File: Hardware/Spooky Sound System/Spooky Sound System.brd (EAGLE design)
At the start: 101.6 x 36.5 mm, 18 parts, among them U1 LM3886TF/NOPB, U2 LM3886TF/NOPB, U3 LM3886TF/NOPB

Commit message: tone control done.
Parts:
- added C10, C17: 220nF, MF_Passives:C0805
- added C11, C18: 47uF, MF_Passives:CP6.3MM
- added C12, C13, C19: 10uF, MF_Passives:CP4MM
- added C14, C7: 2.2nF, MF_Passives:C0805
- added C15, C16, C8, C9: 22nF, MF_Passives:C0805
- added P1, P2, P3: 100K, PP_Passives:DUAL_TAPER_POTENTIOMETER
- added R10: 12K, MF_Passives:R0805
- added R11, R12: 100K, MF_Passives:R0805
- C1, C3, C5: value 47uF -> 0.1uF; device MF_Passives:C0805 -> MF_Passives:C1206
- C2, C4: value 100uF -> 0.1uF; device MF_Passives:CP6.3MM -> MF_Passives:C1206
- C6: value 100uF -> 10uF; device MF_Passives:CP6.3MM -> MF_Passives:CP4MM
- R1, R7: value 1K -> 10K
- R2, R8: value 22K -> 10K
- R3, R9: value 22K -> 4.7K
- R4: value 1K -> 12K
- R5, R6: value 22K -> 100K
- U1: value LM3886TF/NOPB -> TDA7387; device PP_AnalogIC:LM388TF-TO-220-11 -> PP_AnalogIC:TDA7387-FLEXIWATT-25
- U2, U3: value LM3886TF/NOPB -> AZ4558C; device PP_AnalogIC:LM388TF-TO-220-11 -> PP_AnalogIC:AZ4558C_SOIC-8
- moved R7 189.5 mm to (-38.1, -118.1)
- moved U3 180.0 mm to (-31.8, -109.2)
- moved R8 168.1 mm to (-33.0, -118.1)
- moved R9 168.1 mm to (-27.9, -118.1)
- moved C6 100.2 mm to (-3.81, -36.8)
- moved C5 99.6 mm to (2.54, -31.8)
- moved R4 95.6 mm to (-3.81, -54.6)
- moved R6 87.1 mm to (-3.81, -62.2)
- moved R5 81.1 mm to (-3.81, -58.4)
- moved U2 77.8 mm to (6.35, -38.1)
- moved R3 72.4 mm to (-3.81, -50.8)
- moved R2 70.3 mm to (-3.81, -47.0)
- moved C3 64.9 mm to (2.54, -22.9)
- moved C4 60.2 mm to (2.54, -26.7)
- moved R1 53.3 mm to (-3.81, -43.2)
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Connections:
- removed net V+: C2.P$1, C4.P$1, C6.P$1, U1.P$1, U1.P$5, U2.P$1, U2.P$5, U3.P$1, U3.P$5
- new net AC-GND: C5.P$2, U1.P$16
- new net IN_L: U2.3
- new net IN_R: U3.3
- new net N$11: C11.P$1, R5.P$2, R6.P$1, U2.5
- new net N$12: C13.P$2, U3.1, U3.2
- new net N$13: C13.P$1, C14.P$1, R7.P$1
- new net N$14: C16.P$1, P1.1B, R7.P$2
- new net N$15: C16.P$2, C17.P$1, P1.2B, R8.P$2
- new net N$16: C17.P$2, P1.3B, R10.P$2
- new net N$17: R8.P$1, R9.P$2, U3.6
- new net N$18: P2.2B, R9.P$1
- new net N$19: C14.P$2, P2.1B
- new net N$20: C15.P$1, P2.3B
- new net N$21: C15.P$2, C19.P$1, R10.P$1, U3.7
- new net N$22: C18.P$1, R11.P$2, R12.P$1, U3.5
- new net OUT_L: C12.P$2, P3.3A
- new net OUT_R: C19.P$2, P3.1B
- new net TDA7387_IN1: C1.P$2, U1.P$11
- new net TDA7387_IN2: C2.P$2, U1.P$12
- new net TDA7387_IN3: C3.P$2, U1.P$15
- new net TDA7387_IN4: C4.P$2, U1.P$14
- new net VIN: R11.P$1, R5.P$1, U2.8, U3.8
- net GND: now also C11.P$2, C18.P$2, P3.1A, P3.3B, R12.P$2, R6.P$2, U2.4, U3.4; no longer C1.P$2, C2.P$2, C3.P$2, C4.P$2, C5.P$2, C6.P$2, R2.P$2, R5.P$2, R8.P$2, U1.P$7, U1.P$8, U2.P$7, U2.P$8, U3.P$7, U3.P$8
- net N$1: now also C6.P$2, U2.1, U2.2; no longer R1.P$2, R2.P$1, U1.P$10
- net N$10: now also C12.P$1, C8.P$2, R4.P$1, U2.7; no longer C5.P$1, R9.P$2
- net N$2: now also C6.P$1, C7.P$1; no longer R4.P$1, R7.P$1
- net N$3: now also C9.P$1, P1.1A, R1.P$2; no longer R3.P$1, U1.P$9
- net N$4: now also C10.P$1, C9.P$2, P1.2A, R2.P$2; no longer C1.P$1, R3.P$2
- net N$5: now also C10.P$2, P1.3A; no longer R5.P$1, U2.P$10
- net N$6: now also R2.P$1, R3.P$2, U2.6; no longer R6.P$1, U2.P$9
- net N$7: now also P2.2A, R3.P$1; no longer C3.P$1, R6.P$2
- net N$8: now also C7.P$2, P2.1A; no longer R7.P$2, R8.P$1, U3.P$10
- net N$9: now also C8.P$1, P2.3A; no longer R9.P$1, U3.P$9

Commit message: Schematic done. Start Routing.
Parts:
- added C20, C21, C22, C23: 0.01uF, MF_Passives:C1210
- added C24: 22nF, MF_Passives:C0805
- added C25, C27, C28, C31: 10uF, MF_Passives:CP4MM
- added C26: 0.1uF, MF_Passives:C0805
- added C29, C30: 1000uF, MF_Passives:CP12.5MM
- added C32: 47uF, MF_Passives:CP6.3MM
- added C33, C34, C35: 100uF, MF_Passives:CP6.3MM
- added J1: SJ1-3533NS, PP_Connectors:SJ1-3533NS
- added J2, J3, J4: 1546215-2, PP_Connectors:1546215-2
- added P4, P5: 100K, PP_Passives:DUAL_TAPER_POTENTIOMETER
- added R13, R14, R19, R20: 1M, MF_Passives:R0805
- added R15, R16, R17, R18, R21, R22, R23, R24, R27, R30, R31, R32: 0, MF_Passives:R0805
- added R25, R26, R28, R29: 10K, MF_Passives:R0805
- added R33, R34: 220K, MF_Passives:R0805
- added R35: 1K, MF_Passives:R0805
- added U4, U5, U6: AZ4558C, PP_AnalogIC:AZ4558C_SOIC-8
- moved R11 215.6 mm to (96.5, 33.0), turned to 180 degrees
- moved C15 210.1 mm to (96.5, 29.2), turned to 180 degrees
- moved R12 208.6 mm to (91.4, 33.0), turned to 180 degrees
- moved C16 203.0 mm to (91.4, 29.2), turned to 180 degrees
- moved C18 197.9 mm to (95.2, 21.6), turned to 180 degrees
- moved C17 196.2 mm to (86.4, 29.2), turned to 180 degrees
- moved R7 189.6 mm to (81.3, 29.2), turned to 180 degrees
- moved C13 186.8 mm to (88.9, 20.3), turned to 180 degrees
- moved P3 183.7 mm to (83.8, 0.00), turned to 180 degrees
- moved R8 183.4 mm to (76.2, 29.2), turned to 180 degrees
- moved C19 179.6 mm to (83.8, 20.3), turned to 180 degrees
- moved R9 177.5 mm to (71.1, 29.2), turned to 180 degrees
- moved R10 172.1 mm to (66.0, 29.2), turned to 180 degrees
- moved U3 167.8 mm to (74.9, 20.3), turned to 180 degrees
- moved C11 164.0 mm to (95.2, 10.2), turned to 180 degrees
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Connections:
- new net AUD_IN_L: C20.P$1, C22.P$1, J1.2_A, J1.2_B
- new net AUD_IN_R: C21.P$1, C23.P$1, J1.3_A, J1.3_B
- new net L+: J2.P$1, U1.P$9
- new net L-: J2.P$2, U1.P$7
- new net N$23: C27.P$2, R21.P$2, U4.1
- new net N$24: P5.3A, R21.P$1
- new net N$25: P3.3B, R16.P$1
- new net N$26: P3.1B, R17.P$2
- new net N$27: C28.P$2, R23.P$2, U4.7
- new net N$28: P5.3B, R23.P$1
- new net N$29: C26.P$1, R25.P$2, R26.P$2, R28.P$1, U5.2
- new net N$30: C26.P$2, P4.3A, R28.P$2, U5.1
- new net N$31: R29.P$1, U5.3
- new net N$32: P4.2A, R31.P$2
- new net N$33: R30.P$2, R32.P$1, U5.6
- new net N$34: C25.P$1, R30.P$1, U5.7
- new net N$35: P5.2A, U4.2
- new net N$36: P5.1A, R22.P$2
- new net N$37: P5.1B, R24.P$2
- new net N$38: P5.2B, U4.6
- new net N$39: P3.2B, U3.2
- new net N$40: P3.3A, R18.P$2
- new net N$41: P3.2A, U2.2
- new net N$42: P3.1A, R15.P$1
- new net N$43: C24.P$1, R31.P$1, U5.5
- new net N$44: C25.P$2, R27.P$1
- new net N$45: C27.P$1, R26.P$1
- new net N$46: C28.P$1, R25.P$1
- new net N$47: C33.P$2, C34.P$1, R33.P$2, R34.P$1, U6.3
- new net N$48: R35.P$1, U6.1
- new net N$49: C32.P$1, U1.P$10
- new net OUT_SUB: C3.P$1, R27.P$2
- new net R+: J3.P$1, U1.P$5
- new net R-: J3.P$2, U1.P$3
- new net SUB+: J4.P$1, U1.P$17
- new net SUB-: J4.P$2, U1.P$19
- new net SUB_L: C22.P$2, R19.P$1
- new net SUB_R: C23.P$2, R20.P$1, U4.5
- new net VGND: C11.P$2, C18.P$2, C24.P$2, R12.P$2, R13.P$2, R14.P$2, R17.P$1, R18.P$1, R19.P$2, R20.P$2, R22.P$1, R24.P$1, R29.P$2, R32.P$2, R35.P$2, R6.P$2, U6.2
- net GND: now also C29.P$2, C30.P$2, C31.P$2, C32.P$2, C34.P$2, C35.P$2, C4.P$1, C5.P$1, J1.1_A, J1.1_B, J1.S1, J1.S2, J1.S3, J1.S4, J1.S5, J1.S6, R34.P$2, U1.P$1, U1.P$13, U1.P$18, U1.P$2, U1.P$24, U1.P$8, U4.4, U5.4, U6.4; no longer C11.P$2, C18.P$2, P3.1A, P3.3B, R12.P$2, R6.P$2
- net IN_L: now also C20.P$2, R14.P$1
- net IN_R: now also C21.P$2, R13.P$1
- net N$1: now also R15.P$2; no longer U2.2
- net N$12: now also R16.P$2; no longer U3.2
- net OUT_L: now also C1.P$1; no longer P3.3A
- net OUT_R: now also C2.P$1; no longer P3.1B
- net VIN: now also C29.P$1, C30.P$1, C31.P$1, C33.P$1, C35.P$1, R33.P$1, U1.P$20, U1.P$22, U1.P$4, U1.P$6, U4.8, U5.8, U6.8
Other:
- board size 101.6 x 36.5 mm -> 101.6 x 54.3 mm

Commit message: Starting layout...
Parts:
- added J5: 1546215-2, PP_Connectors:1546215-2
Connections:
- net GND: now also J5.P$2
- net VIN: now also J5.P$1
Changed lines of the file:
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@@
 <attribute name="MPN" value="" x="97.79" y="48.26" size="1.778" layer="27" rot="R180" display="off"/>
+</element>
+<element name="J5" library="PP_Connectors" package="1546215-2" value="1546215-2" x="3.81" y="50.8" rot="R180">
+<attribute name="URL" value="" x="3.81" y="50.8" size="1.778" layer="27" rot="R180" display="off"/>
+<attribute name="POPULATE" value="1" x="3.81" y="50.8" size="1.778" layer="27" rot="R180" display="off"/>
+<attribute name="LABEL02" value="GND" x="3.81" y="50.8" size="1.778" layer="27" rot="R180" display="off"/>
+<attribute name="HOUSEPART" value="" x="3.81" y="50.8" size="1.778" layer="27" rot="R180" display="off"/>
+<attribute name="LABEL01" value="VIN" x="3.81" y="50.8" size="1.778" layer="27" rot="R180" display="off"/>
+<attribute name="MPN" value="" x="3.81" y="50.8" size="1.778" layer="27" rot="R180" display="off"/>
 </element>
 </elements>
@@
 <contactref element="C30" pad="P$1"/>
 <contactref element="U1" pad="P$20"/>
-<wire x1="58.42" y1="36.99" x2="73.66" y2="36.99" width="0" layer="19" extent="1-1"/>
+<contactref element="J5" pad="P$1"/>
+<wire x1="90.805" y1="23.02" x2="97.47" y2="33.02" width="0" layer="19" extent="1-1"/>
+<wire x1="72.23" y1="18.415" x2="90.805" y2="23.02" width="0" layer="19" extent="1-1"/>
+<wire x1="61.214" y1="31.9278" x2="72.23" y2="18.415" width="0" layer="19" extent="1-1"/>
+<wire x1="59.182" y1="31.9278" x2="61.214" y2="31.9278" width="0" layer="19" extent="1-1"/>
+<wire x1="58.42" y1="36.99" x2="59.182" y2="31.9278" width="0" layer="19" extent="1-1"/>
+<wire x1="73.66" y1="36.99" x2="61.214" y2="31.9278" width="0" layer="19" extent="1-1"/>
 <wire x1="44.45" y1="37.31" x2="58.42" y2="36.99" width="0" layer="19" extent="1-1"/>
-<wire x1="34.29" y1="35.33" x2="44.45" y2="37.31" width="0" layer="19" extent="1-1"/>
-<wire x1="19.05" y1="31.52" x2="34.29" y2="35.33" width="0" layer="19" extent="1-1"/>
+<wire x1="44.958" y1="31.9278" x2="44.45" y2="37.31" width="0" layer="19" extent="1-1"/>
+<wire x1="42.926" y1="31.9278" x2="44.958" y2="31.9278" width="0" layer="19" extent="1-1"/>
+<wire x1="34.29" y1="35.33" x2="42.926" y2="31.9278" width="0" layer="19" extent="1-1"/>
+<wire x1="40.005" y1="23.02" x2="42.926" y2="31.9278" width="0" layer="19" extent="1-1"/>
+<wire x1="29.21" y1="20.64" x2="40.005" y2="23.02" width="0" layer="19" extent="1-1"/>
+<wire x1="19.05" y1="31.52" x2="29.21" y2="20.64" width="0" layer="19" extent="1-1"/>
 <wire x1="9.84" y1="30.48" x2="19.05" y2="31.52" width="0" layer="19" extent="1-1"/>
+<wire x1="6.985" y1="34.45" x2="9.84" y2="30.48" width="0" layer="19" extent="1-1"/>
 <wire x1="2.38" y1="23.495" x2="9.84" y2="30.48" width="0" layer="19" extent="1-1"/>
-<wire x1="90.805" y1="23.02" x2="2.38" y2="23.495" width="0" layer="19" extent="1-1"/>
-<wire x1="40.005" y1="23.02" x2="90.805" y2="23.02" width="0" layer="19" extent="1-1"/>
-<wire x1="97.47" y1="33.02" x2="40.005" y2="23.02" width="0" layer="19" extent="1-1"/>
-<wire x1="72.23" y1="18.415" x2="97.47" y2="33.02" width="0" layer="19" extent="1-1"/>
-<wire x1="29.21" y1="20.64" x2="72.23" y2="18.415" width="0" layer="19" extent="1-1"/>
-<wire x1="6.985" y1="34.45" x2="29.21" y2="20.64" width="0" layer="19" extent="1-1"/>
-<wire x1="44.958" y1="31.9278" x2="6.985" y2="34.45" width="0" layer="19" extent="1-1"/>
-<wire x1="42.926" y1="31.9278" x2="44.958" y2="31.9278" width="0" layer="19" extent="1-1"/>
-<wire x1="59.182" y1="31.9278" x2="44.958" y2="31.9278" width="0" layer="19" extent="1-1"/>
-<wire x1="61.214" y1="31.9278" x2="59.182" y2="31.9278" width="0" layer="19" extent="1-1"/>
+<wire x1="5.08" y1="50.8" x2="2.38" y2="23.495" width="0" layer="19" extent="1-1"/>
 </signal>
 <signal name="N$1">
@@
 <contactref element="J1" pad="1_A"/>
 <contactref element="J1" pad="1_B"/>
+<contactref element="J5" pad="P$2"/>
 <wire x1="71.04" y1="51.54" x2="71.04" y2="51.54" width="0" layer="19" extent="1-16"/>
 <wire x1="72.04" y1="47.39" x2="71.04" y2="51.54" width="0" layer="19" extent="1-16"/>
@@
 <wire x1="62.14" y1="42.94" x2="62.14" y2="51.54" width="0" layer="19" extent="1-16"/>
 <wire x1="62.14" y1="42.94" x2="62.14" y2="42.94" width="0" layer="19" extent="1-16"/>
-<wire x1="66.04" y1="31.59" x2="62.14" y2="42.94" width="0" layer="19" extent="1-16"/>
+<wire x1="63.246" y1="31.9278" x2="62.14" y2="42.94" width="0" layer="19" extent="16-16"/>
+<wire x1="66.04" y1="31.59" x2="63.246" y2="31.9278" width="0" layer="19" extent="1-1"/>
+<wire x1="57.15" y1="31.9278" x2="63.246" y2="31.9278" width="0" layer="19" extent="1-1"/>
+<wire x1="50.8" y1="31.59" x2="57.15" y2="31.9278" width="0" layer="19" extent="1-1"/>
+<wire x1="46.99" y1="31.9278" x2="50.8" y2="31.59" width="0" layer="19" extent="1-1"/>
+<wire x1="44.45" y1="33.81" x2="46.99" y2="31.9278" width="0" layer="19" extent="1-1"/>
+<wire x1="52.07" y1="27.94" x2="50.8" y2="31.59" width="0" layer="19" extent="1-1"/>
+<wire x1="40.894" y1="31.9278" x2="44.45" y2="33.81" width="0" layer="19" extent="1-1"/>
+<wire x1="39.878" y1="27.94" x2="40.894" y2="31.9278" width="0" layer="19" extent="1-1"/>
+<wire x1="34.29" y1="25.63" x2="39.878" y2="27.94" width="0" layer="19" extent="1-1"/>
 <wire x1="73.66" y1="31.59" x2="66.04" y2="31.59" width="0" layer="19" extent="1-1"/>
-<wire x1="50.8" y1="31.59" x2="66.04" y2="31.59" width="0" layer="19" extent="1-1"/>
-<wire x1="44.45" y1="33.81" x2="50.8" y2="31.59" width="0" layer="19" extent="1-1"/>
-<wire x1="34.29" y1="25.63" x2="44.45" y2="33.81" width="0" layer="19" extent="1-1"/>
+<wire x1="77.63" y1="22.225" x2="73.66" y2="31.59" width="0" layer="19" extent="1-1"/>
+<wire x1="43.815" y1="17.62" x2="39.878" y2="27.94" width="0" layer="19" extent="1-1"/>
 <wire x1="19.05" y1="21.82" x2="34.29" y2="25.63" width="0" layer="19" extent="1-1"/>
-<wire x1="7.78" y1="27.305" x2="19.05" y2="21.82" width="0" layer="19" extent="1-1"/>
-<wire x1="7.94" y1="34.29" x2="7.78" y2="27.305" width="0" layer="19" extent="1-1"/>
-<wire x1="94.615" y1="17.62" x2="7.78" y2="27.305" width="0" layer="19" extent="1-1"/>
-<wire x1="43.815" y1="17.62" x2="94.615" y2="17.62" width="0" layer="19" extent="1-1"/>
-<wire x1="77.63" y1="22.225" x2="43.815" y2="17.62" width="0" layer="19" extent="1-1"/>
-<wire x1="10.795" y1="29.05" x2="77.63" y2="22.225" width="0" layer="19" extent="1-1"/>
-<wire x1="2.54" y1="26.49" x2="10.795" y2="29.05" width="0" layer="19" extent="1-1"/>
+<wire x1="10.795" y1="29.05" x2="19.05" y2="21.82" width="0" layer="19" extent="1-1"/>
+<wire x1="7.78" y1="27.305" x2="10.795" y2="29.05" width="0" layer="19" extent="1-1"/>
+<wire x1="2.54" y1="26.49" x2="7.78" y2="27.305" width="0" layer="19" extent="1-1"/>
+<wire x1="7.94" y1="34.29" x2="10.795" y2="29.05" width="0" layer="19" extent="1-1"/>
+<wire x1="94.615" y1="17.62" x2="77.63" y2="22.225" width="0" layer="19" extent="1-1"/>
 <wire x1="3.63" y1="3.81" x2="2.54" y2="26.49" width="0" layer="19" extent="1-1"/>
-<wire x1="39.878" y1="27.94" x2="3.63" y2="3.81" width="0" layer="19" extent="1-1"/>
-<wire x1="40.894" y1="31.9278" x2="39.878" y2="27.94" width="0" layer="19" extent="1-1"/>
-<wire x1="46.99" y1="31.9278" x2="40.894" y2="31.9278" width="0" layer="19" extent="1-1"/>
-<wire x1="52.07" y1="27.94" x2="46.99" y2="31.9278" width="0" layer="19" extent="1-1"/>
-<wire x1="57.15" y1="31.9278" x2="52.07" y2="27.94" width="0" layer="19" extent="1-1"/>
-<wire x1="63.246" y1="31.9278" x2="57.15" y2="31.9278" width="0" layer="19" extent="1-1"/>
+<wire x1="2.54" y1="50.8" x2="3.63" y2="3.81" width="0" layer="19" extent="1-1"/>
 </signal>
 <signal name="N$47">

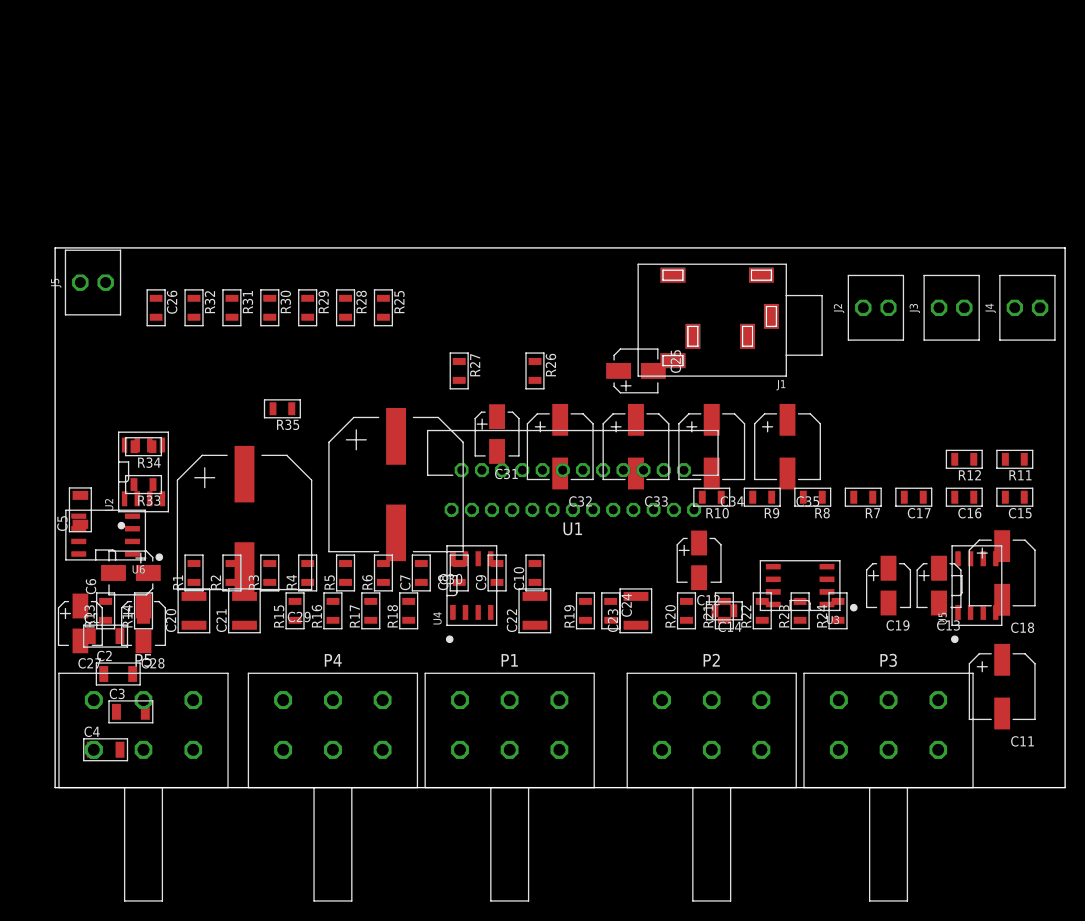
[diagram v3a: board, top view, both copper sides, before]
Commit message: Parts layed out
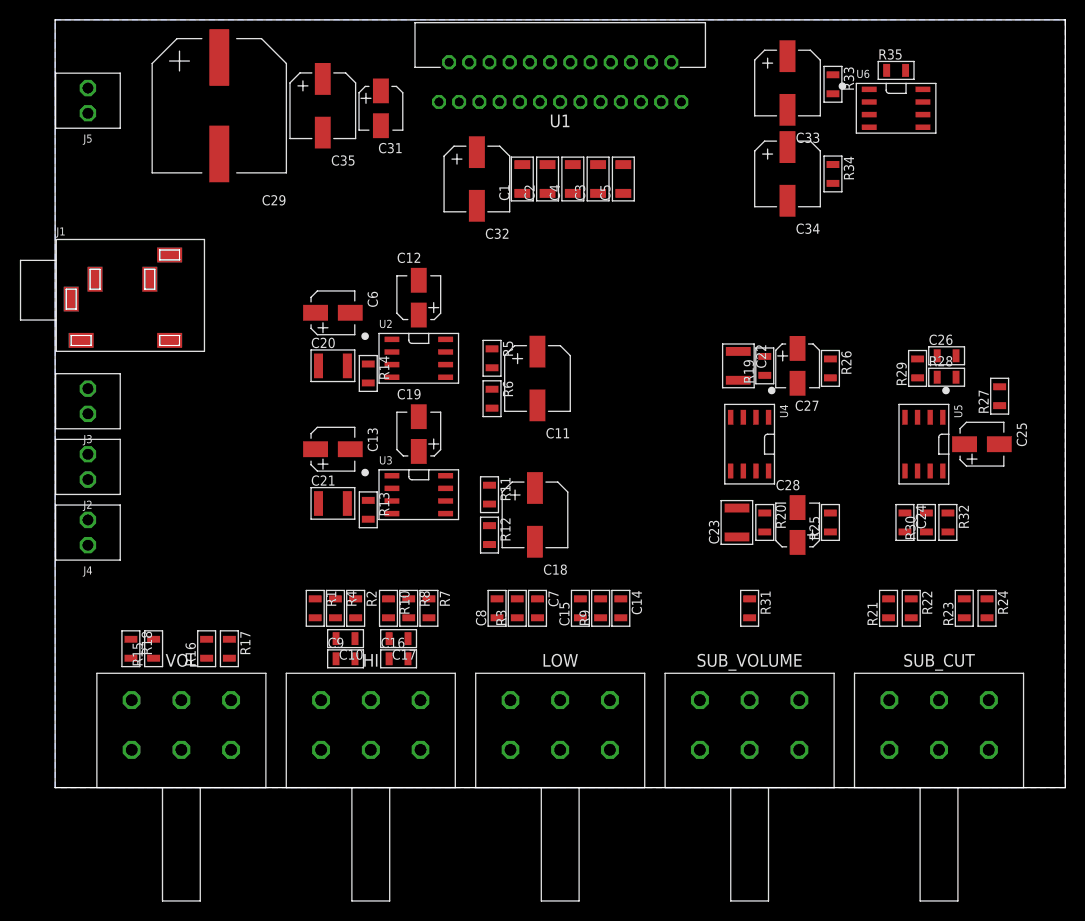
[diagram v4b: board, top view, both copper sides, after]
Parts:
- removed C30: 1000uF, MF_Passives:CP12.5MM
- removed P1, P2, P3, P4, P5: 100K, PP_Passives:DUAL_TAPER_POTENTIOMETER
- added HI, LOW, SUB_CUT, SUB_VOLUME, VOL: 100K, PP_Passives:DUAL_TAPER_POTENTIOMETER
- moved J4 97.2 mm to (3.30, 25.7), turned to 270 degrees
- moved U6 90.4 mm to (84.6, 68.3), turned to 0 degrees
- moved J3 87.4 mm to (3.30, 38.9), turned to 270 degrees
- moved J2 80.8 mm to (3.30, 32.3), turned to 270 degrees
- moved R33 80.2 mm to (78.2, 70.7), turned to 270 degrees
- moved C26 79.6 mm to (89.7, 43.4), turned to 0 degrees
- moved R32 78.8 mm to (89.8, 26.7)
- moved C27 76.6 mm to (74.7, 42.4)
- moved R34 74.6 mm to (78.2, 61.7), turned to 270 degrees
- moved C4 74.2 mm to (52.1, 61.2), turned to 90 degrees
- moved C3 71.3 mm to (54.6, 61.2), turned to 90 degrees
- moved R35 70.5 mm to (84.6, 72.1), turned to 0 degrees
- moved R30 69.5 mm to (87.6, 26.7), turned to 90 degrees
- moved C28 66.5 mm to (74.7, 26.4), turned to 0 degrees
- moved C2 65.9 mm to (49.5, 61.2), turned to 90 degrees
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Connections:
- net GND: no longer C30.P$2
- net N$14: now also HI.1B; no longer P1.1B
- net N$15: now also HI.2B; no longer P1.2B
- net N$16: now also HI.3B; no longer P1.3B
- net N$18: now also LOW.2B; no longer P2.2B
- net N$19: now also LOW.1B; no longer P2.1B
- net N$20: now also LOW.3B; no longer P2.3B
- net N$24: now also SUB_CUT.3A; no longer P5.3A
- net N$25: now also VOL.3B; no longer P3.3B
- net N$26: now also VOL.1B; no longer P3.1B
- net N$28: now also SUB_CUT.3B; no longer P5.3B
- net N$3: now also HI.1A; no longer P1.1A
- net N$30: now also SUB_VOLUME.3A; no longer P4.3A
- net N$32: now also SUB_VOLUME.2A; no longer P4.2A
- net N$35: now also SUB_CUT.2A; no longer P5.2A
- net N$36: now also SUB_CUT.1A; no longer P5.1A
- net N$37: now also SUB_CUT.1B; no longer P5.1B
- net N$38: now also SUB_CUT.2B; no longer P5.2B
- net N$39: now also VOL.2B; no longer P3.2B
- net N$4: now also HI.2A; no longer P1.2A
- net N$40: now also VOL.3A; no longer P3.3A
- net N$41: now also VOL.2A; no longer P3.2A
- net N$42: now also VOL.1A; no longer P3.1A
- net N$5: now also HI.3A; no longer P1.3A
- net N$7: now also LOW.2A; no longer P2.2A
- net N$8: now also LOW.1A; no longer P2.1A
- net N$9: now also LOW.3A; no longer P2.3A
- net SUB_L: now also U4.3
- net VIN: no longer C30.P$1
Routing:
- added copper zone on layer 16, net GND
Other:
- board size 101.6 x 54.3 mm -> 101.6 x 77.2 mm
